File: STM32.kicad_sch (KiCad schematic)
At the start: 44 parts, among them IC201 ESDALC6V1W5, IC202 ESDALC6V1W5, IC203 ESDALC6V1W5, Q201 DMG1012T-13, Q202 DMG1012T-13, Q203 DMG1012T-13, Q204 DMG1012T-13, SW1 SW_SPDT, U201 TLV9304IDR, U202 STM32U575ZIT6Q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

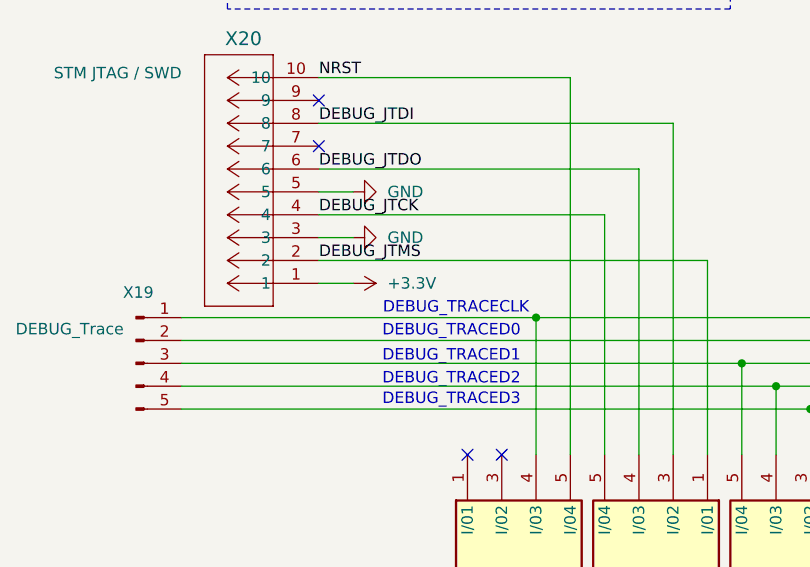
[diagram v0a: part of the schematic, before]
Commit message: Add board housing STEP files; update KiCad files
Add exported mechanical STEP models for the board housing (CAD/board_housing.step and variants _o, _stg, _u). Also update KiCad project assets and documentation: POWER_CONTROL.md, Power.kicad_sch, STM32.kicad_sch, uC_Agri-PV.kicad_pcb, uC_Agri-PV.kicad_pro, uC_Agri-PV.net, bom/ibom.html and fp-info-cache. These changes synchronize the PCB/schematic/BOM with the new mechanical exports and refresh power/control documentation and footprint cache. Layout is not finished jet.
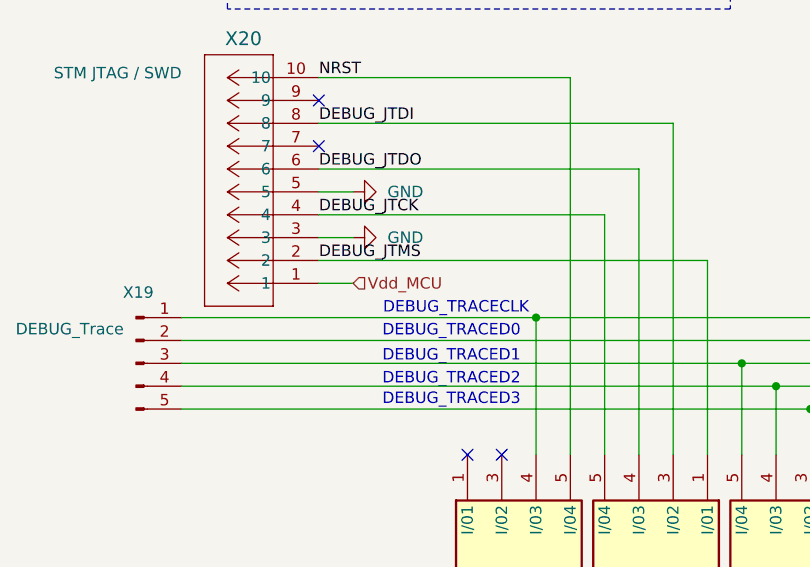
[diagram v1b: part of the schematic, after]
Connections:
- net +3.3V: no longer X20.1
- net Vdd_MCU: now also X20.1
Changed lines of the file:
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@@
+		)
+	)
+	(hierarchical_label "Vdd_MCU"
+		(shape input)
+		(at 53.34 165.1 0)
+		(effects
+			(font
+				(size 1.27 1.27)
+			)
+			(justify left)
 		)
 	)
@@
 					(unit 1)
 				)
-			)
-		)
-	)
-	(symbol
-		(lib_id "power:+3.3V")
-		(at 53.34 165.1 270)
-		(unit 1)
-		(exclude_from_sim no)
-		(in_bom yes)
-		(on_board yes)
-		(dnp no)
-		(fields_autoplaced yes)
-		(property "Reference" "#PWR0203"
-			(at 49.53 165.1 0)
-			(effects
-				(font
-					(size 1.27 1.27)
-				)
-				(hide yes)
-			)
-		)
-		(property "Value" "+3.3V"
-			(at 57.15 165.0999 90)
-			(effects
-				(font
-					(size 1.27 1.27)
-				)
-				(justify left)
-			)
-		)
-		(property "Footprint" ""
-			(at 53.34 165.1 0)
-			(effects
-				(font
-					(size 1.27 1.27)
-				)
-				(hide yes)
-			)
-		)
-		(property "Datasheet" ""
-			(at 53.34 165.1 0)
-			(effects
-				(font
-					(size 1.27 1.27)
-				)
-				(hide yes)
-			)
-		)
-		(property "Description" "Power symbol creates a global label with name \"+3.3V\""
-			(at 53.34 165.1 0)
-			(effects
-				(font
-					(size 1.27 1.27)
-				)
-				(hide yes)
-			)
-		)
-		(pin "1"
-		)
-		(instances
-			(project ""
-				(path "/69abffa1-550c-4cd8-ae80-a1755923d6dc/68eeaf65-50b7-4f21-91a4-9a8eefc615e6"
-					(reference "#PWR0203")
-					(unit 1)
-				)

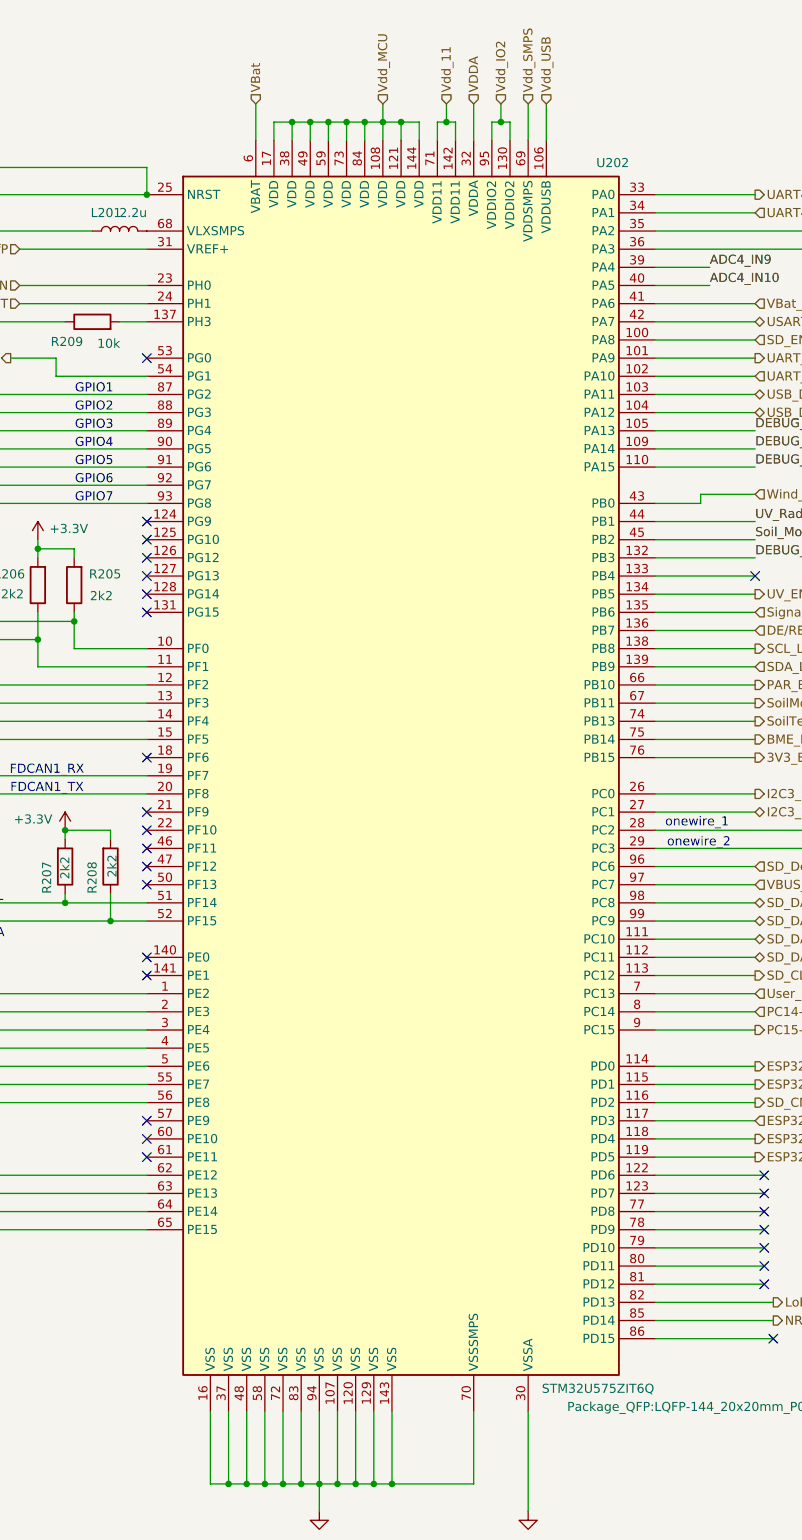
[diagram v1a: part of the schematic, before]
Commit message: Add SamacSys & CAPPRD library; update KiCad
Add a new SamacSys parts library and a complete CAPPRD500 footprint/package set (870585375004) with multi-EDA exports and 3D STEP models. Also add sym-lib-table and SamacSys parts entries, and update KiCad project files (schematics, PCB, project file and generated PDFs) to reference the new parts and footprints.
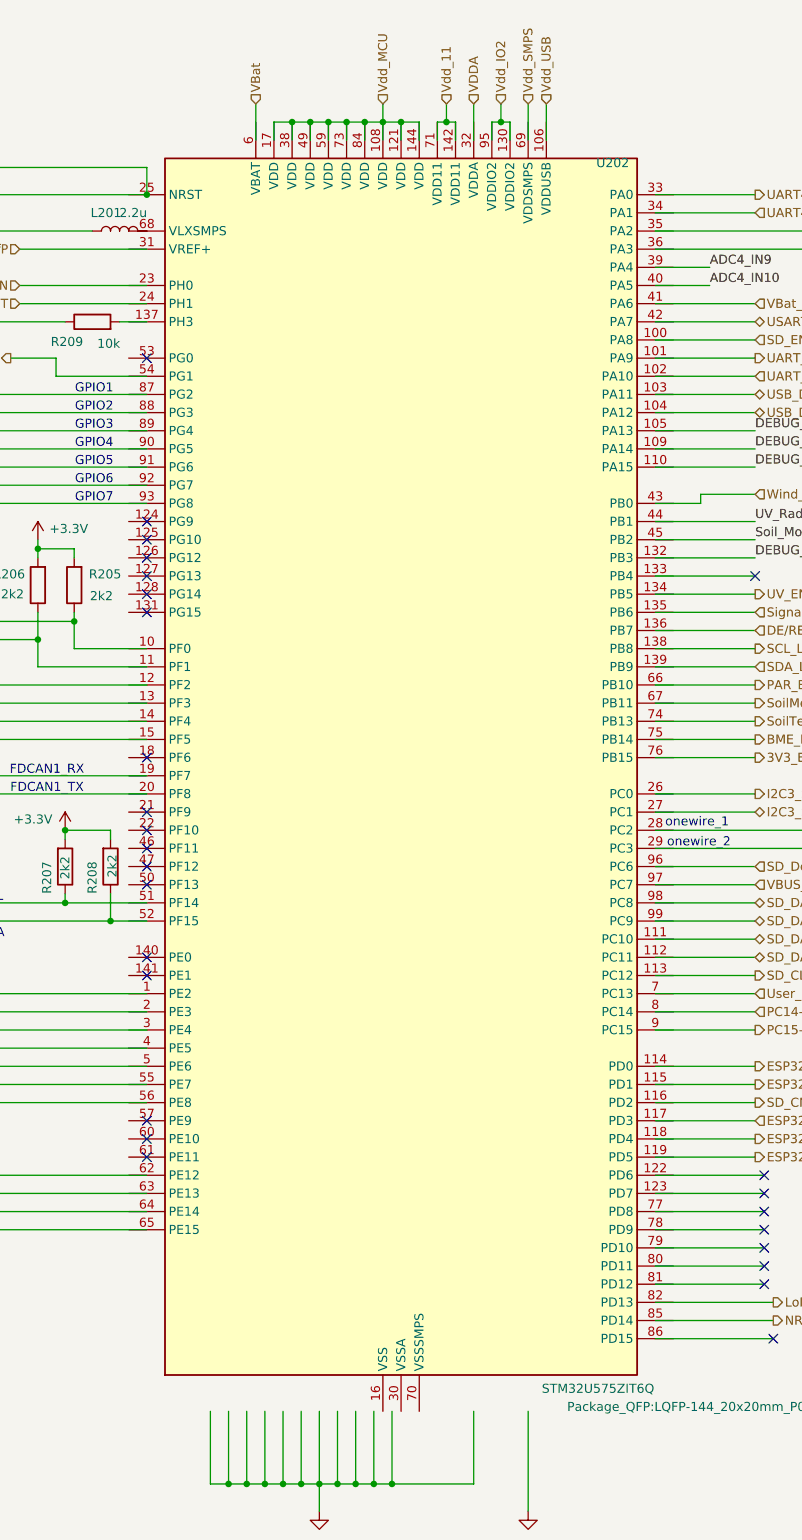
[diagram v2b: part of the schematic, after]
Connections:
- net 3V3_EN: no longer U202.76 (PB15)
- net 3V3_OPV_EN: no longer U202.54 (PG1)
- net ADC4_IN10: no longer U202.40 (PA5)
- net ADC4_IN9: no longer U202.39 (PA4)
- net BME_EN: no longer U202.75 (PB14)
- net DEBUG_JTCK: no longer U202.109 (PA14)
- net DEBUG_JTDI: no longer U202.110 (PA15)
- net DEBUG_JTDO: no longer U202.132 (PB3)
- net DEBUG_JTMS: no longer U202.105 (PA13)
- net DE/RE: no longer U202.136 (PB7)
- net ESP32_EN: no longer U202.119 (PD5)
- net ESP32_MISO: no longer U202.117 (PD3)
- net ESP32_MOSI: no longer U202.118 (PD4)
- net ESP32_NSS: no longer U202.114 (PD0)
- net ESP32_SCK: no longer U202.115 (PD1)
- net GND: no longer U202.107 (VSS), U202.120 (VSS), U202.129 (VSS), U202.143 (VSS), U202.16 (VSS), U202.37 (VSS), U202.48 (VSS), U202.58 (VSS), U202.70 (VSSSMPS), U202.72 (VSS), U202.83 (VSS), U202.94 (VSS)
- net GNDA: no longer U202.30 (VSSA)
- net I2C3_SCL: no longer U202.26 (PC0)
- net I2C3_SDA: no longer U202.27 (PC1)
- net LED1: no longer U202.56 (PE8)
- net LED2: no longer U202.55 (PE7)
- net LoRa_EN: no longer U202.82 (PD13)
- net MISO_LoRa: no longer U202.64 (PE14)
- net MOSI_LoRa: no longer U202.65 (PE15)
- net NRST: no longer U202.25 (NRST)
- net NRST2: no longer U202.85 (PD14)
- net NSS_LoRa: no longer U202.62 (PE12)
- net PAR_EN: no longer U202.66 (PB10)
- net PC14-OSC32_IN: no longer U202.8 (PC14)
- net PC15-OSC32_OUT: no longer U202.9 (PC15)
- net RCC_OSC_IN: no longer U202.23 (PH0)
- net RCC_OSC_OUT: no longer U202.24 (PH1)
- net SCK_LoRa: no longer U202.63 (PE13)
- net SCL_LoRa: no longer U202.138 (PB8)
- net SDA_LoRa: no longer U202.139 (PB9)
- net SD_CLK: no longer U202.113 (PC12)
- net SD_CMD: no longer U202.116 (PD2)
- net SD_DAT0: no longer U202.98 (PC8)
- net SD_DAT1: no longer U202.99 (PC9)
- net SD_DAT2: no longer U202.111 (PC10)
- net SD_DAT3: no longer U202.112 (PC11)
- net SD_Detect: no longer U202.96 (PC6)
- net SD_EN: no longer U202.100 (PA8)
- net Signal_wind_velocity: no longer U202.135 (PB6)
- net SoilMoist_EN: no longer U202.67 (PB11)
- net SoilTemp_EN: no longer U202.74 (PB13)
- net Soil_Moisture: no longer U202.45 (PB2)
- net UART4_RX: no longer U202.34 (PA1)
- net UART4_TX: no longer U202.33 (PA0)
- net UART_RX: no longer U202.102 (PA10)
- net UART_TX: no longer U202.101 (PA9)
- net USART2_ONEWIRE: no longer U202.42 (PA7)
- net USB_D+: no longer U202.104 (PA12)
- net USB_D-: no longer U202.103 (PA11)
- net UV_EN: no longer U202.134 (PB5)
- net UV_Radiation: no longer U202.44 (PB1)
- net User_Button: no longer U202.7 (PC13)
- net VBUS_SENSE: no longer U202.97 (PC7)
- net VBat: no longer U202.6 (VBAT)
- net VBat_meas: no longer U202.41 (PA6)
- net VDDA: no longer U202.32 (VDDA)
- net VRefP: no longer U202.31 (VREF+)
- net Vdd_SMPS: no longer U202.69 (VDDSMPS)
- net Vdd_USB: no longer U202.106 (VDDUSB)
- net Wind_EN: no longer U202.43 (PB0)
- net at L201.2: no longer U202.68 (VLXSMPS)
- net at X10.1 (Pin_1): no longer U202.28 (PC2)
- net at X10.2 (Pin_2): no longer U202.29 (PC3)
- net at R206.1, X9.3 (Pin_3): no longer U202.11 (PF1)
- net at R205.1, X9.2 (Pin_2): no longer U202.10 (PF0)
- net at Q203.1 (G): no longer U202.14 (PF4)
- net at X5.1 (Pin_1): no longer U202.93 (PG8)
- net at X5.2 (Pin_2): no longer U202.92 (PG7)
- net at X5.3 (Pin_3): no longer U202.91 (PG6)
- net at X5.4 (Pin_4): no longer U202.90 (PG5)
- net at X5.5 (Pin_5): no longer U202.89 (PG4)
- net at X5.6 (Pin_6): no longer U202.88 (PG3)
- net at X5.7 (Pin_7): no longer U202.87 (PG2)
- net at Q201.1 (G): no longer U202.12 (PF2)
- net at IC201.4 (I/03), X19.1 (Pin_1): no longer U202.1 (PE2)
- net at U202.13 (PF3): no longer Q202.1 (G)
- net at U202.137 (PH3): no longer R209.2
- net at U202.15 (PF5): no longer Q204.1 (G)
- net at U202.19 (PF7): no longer X8.2 (Pin_2)
- net at IC203.1 (I/01), X19.2 (Pin_2): no longer U202.2 (PE3)
- net at U202.20 (PF8): no longer X8.3 (Pin_3)
- net at IC203.5 (I/04), X19.3 (Pin_3): no longer U202.3 (PE4)
- net at U202.35 (PA2): no longer X7.2 (Pin_2)
- net at U202.36 (PA3): no longer X7.3 (Pin_3)
- net at IC203.4 (I/03), X19.4 (Pin_4): no longer U202.4 (PE5)
- net at IC203.3 (I/02), X19.5 (Pin_5): no longer U202.5 (PE6)
- net at R207.1, X4.3 (Pin_3): no longer U202.51 (PF14)
- net at R208.1, X4.2 (Pin_2): no longer U202.52 (PF15)
- new net: U202.107 (VSS), U202.120 (VSS), U202.129 (VSS), U202.143 (VSS), U202.16 (VSS), U202.37 (VSS), U202.48 (VSS), U202.58 (VSS), U202.72 (VSS), U202.83 (VSS), U202.94 (VSS)
